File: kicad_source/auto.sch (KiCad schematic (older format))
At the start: 24 parts, among them U14 NE555, U15 74xx175, U16 74xx00, U17 74xx175, U18 74xx32, U3 74xx08

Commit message: added pause mode for automate
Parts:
- U14: symbol IC_logic:NE555 -> SonarExtenderI2C-rescue:NE555-IC_logic
- U15, U17: symbol IC_logic:74xx175 -> SonarExtenderI2C-rescue:74xx175-IC_logic
- U16: symbol IC_logic:74xx00 -> SonarExtenderI2C-rescue:74xx00-IC_logic
- U18: symbol IC_logic:74xx32 -> SonarExtenderI2C-rescue:74xx32-IC_logic
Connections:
- net labels added: AUTOEN, PAUSE
- net labels removed: CNT0, CNT1, CNT2, CNT3
- wire segments 175 -> 170
- no-connect marks 5 -> 11
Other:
- moved on the sheet: C15, C16, C17, C21, R3, R4, U3

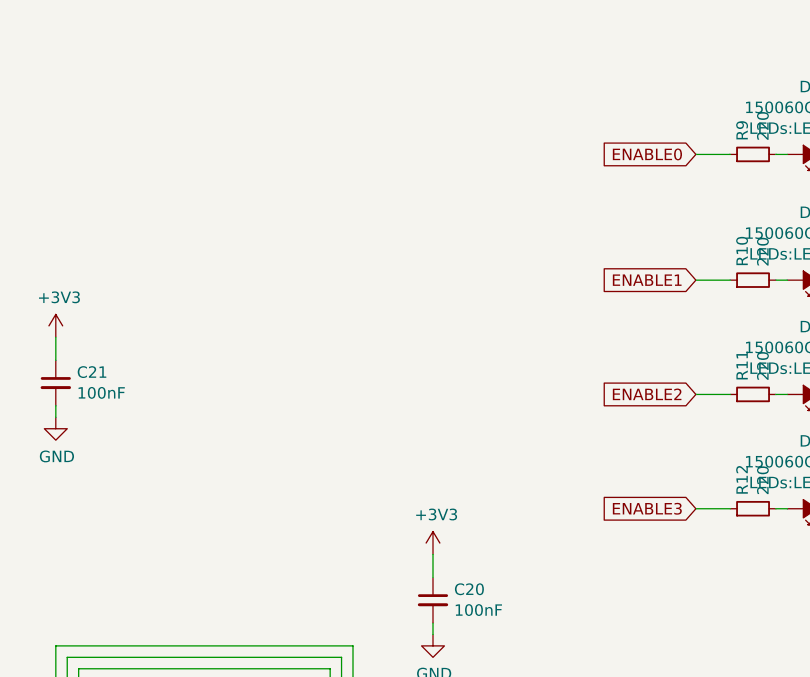
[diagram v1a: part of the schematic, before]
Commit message: added EN LEDS
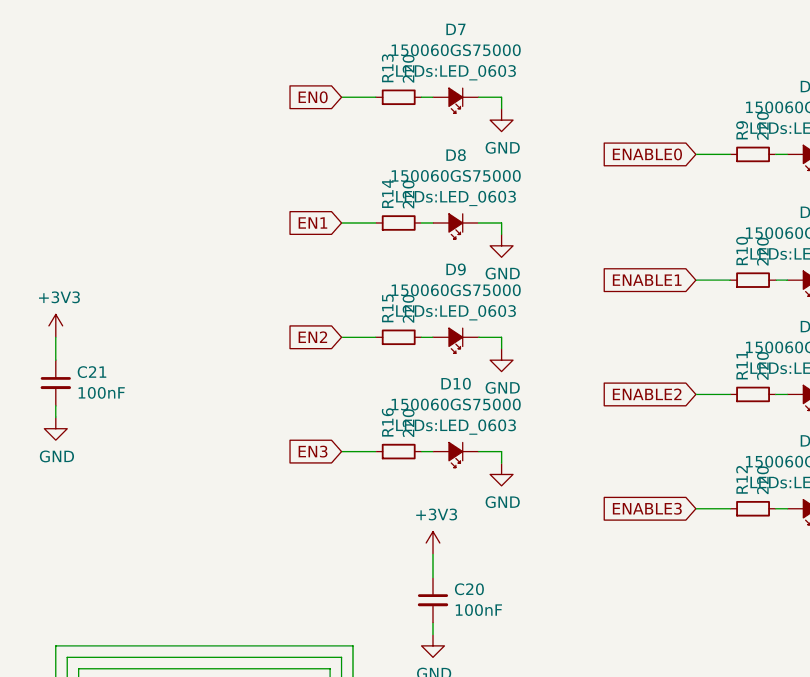
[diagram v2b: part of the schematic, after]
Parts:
- added D10, D7, D8, D9: 150060GS75000, LEDs:LED_0603, symbol devices:Led_Small
- added R13, R14, R15, R16: 220, resistors:R_0603, symbol devices:R_0603
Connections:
- wire segments 170 -> 186
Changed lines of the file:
@@
 NoConn ~ 3550 2500
 NoConn ~ 3550 2300
+$Comp
+L devices:R_0603 R?
+U 1 1 5F04A413
+P 8150 950
+AR Path="/5F04A413" Ref="R?"  Part="1"
+AR Path="/5EDDA6D0/5F04A413" Ref="R13"  Part="1"
+F 0 "R13" H 8209 996 50  0000 L CNN
+F 1 "220" H 8209 905 50  0000 L CNN
+F 2 "resistors:R_0603" H 8150 800 50  0001 C CNN
+F 3 "" H 8150 950 50  0000 C CNN
+	1    8150 950
+	0    -1   -1   0
+$EndComp
+Wire Wire Line
+	8300 950  8250 950
+$Comp
+L power-supply:GND #PWR?
+U 1 1 5F04A41A
+P 8600 1000
+AR Path="/5F04A41A" Ref="#PWR?"  Part="1"
+AR Path="/5EDDA6D0/5F04A41A" Ref="#PWR0132"  Part="1"
+F 0 "#PWR0132" H 8600 750 50  0001 C CNN
+F 1 "GND" H 8605 827 50  0000 C CNN
+F 2 "" H 8600 1000 50  0000 C CNN
+F 3 "" H 8600 1000 50  0000 C CNN
+	1    8600 1000
+	1    0    0    -1
+$EndComp
+Wire Wire Line
+	8600 950  8600 1000
+Wire Wire Line
+	8500 950  8600 950
+$Comp
+L devices:R_0603 R?
+U 1 1 5F04A422
+P 8150 1500
+AR Path="/5F04A422" Ref="R?"  Part="1"
+AR Path="/5EDDA6D0/5F04A422" Ref="R14"  Part="1"
+F 0 "R14" H 8209 1546 50  0000 L CNN
+F 1 "220" H 8209 1455 50  0000 L CNN
+F 2 "resistors:R_0603" H 8150 1350 50  0001 C CNN
+F 3 "" H 8150 1500 50  0000 C CNN
+	1    8150 1500
+	0    -1   -1   0
+$EndComp
+Wire Wire Line
+	8300 1500 8250 1500
+$Comp
+L power-supply:GND #PWR?
+U 1 1 5F04A429
+P 8600 1550
+AR Path="/5F04A429" Ref="#PWR?"  Part="1"
+AR Path="/5EDDA6D0/5F04A429" Ref="#PWR0133"  Part="1"
+F 0 "#PWR0133" H 8600 1300 50  0001 C CNN
+F 1 "GND" H 8605 1377 50  0000 C CNN
+F 2 "" H 8600 1550 50  0000 C CNN
+F 3 "" H 8600 1550 50  0000 C CNN
+	1    8600 1550
+	1    0    0    -1
+$EndComp
+Wire Wire Line
+	8600 1500 8600 1550
+Wire Wire Line
+	8500 1500 8600 1500
+$Comp
+L devices:R_0603 R?
+U 1 1 5F04A431
+P 8150 2000
+AR Path="/5F04A431" Ref="R?"  Part="1"
+AR Path="/5EDDA6D0/5F04A431" Ref="R15"  Part="1"
+F 0 "R15" H 8209 2046 50  0000 L CNN
+F 1 "220" H 8209 1955 50  0000 L CNN
+F 2 "resistors:R_0603" H 8150 1850 50  0001 C CNN
+F 3 "" H 8150 2000 50  0000 C CNN
+	1    8150 2000
+	0    -1   -1   0
+$EndComp
+Wire Wire Line
+	8300 2000 8250 2000
+$Comp
+L power-supply:GND #PWR?
+U 1 1 5F04A438
+P 8600 2050
+AR Path="/5F04A438" Ref="#PWR?"  Part="1"
+AR Path="/5EDDA6D0/5F04A438" Ref="#PWR0134"  Part="1"
+F 0 "#PWR0134" H 8600 1800 50  0001 C CNN
+F 1 "GND" H 8605 1877 50  0000 C CNN
+F 2 "" H 8600 2050 50  0000 C CNN
+F 3 "" H 8600 2050 50  0000 C CNN
+	1    8600 2050
+	1    0    0    -1
+$EndComp
+Wire Wire Line
+	8600 2000 8600 2050
+Wire Wire Line
+	8500 2000 8600 2000
+$Comp
+L devices:R_0603 R?
+U 1 1 5F04A440
+P 8150 2500
+AR Path="/5F04A440" Ref="R?"  Part="1"
+AR Path="/5EDDA6D0/5F04A440" Ref="R16"  Part="1"
+F 0 "R16" H 8209 2546 50  0000 L CNN
+F 1 "220" H 8209 2455 50  0000 L CNN
+F 2 "resistors:R_0603" H 8150 2350 50  0001 C CNN
+F 3 "" H 8150 2500 50  0000 C CNN
+	1    8150 2500
+	0    -1   -1   0
+$EndComp
+$Comp
+L devices:Led_Small D?
+U 1 1 5F04A446
+P 8400 2500
+AR Path="/5F04A446" Ref="D?"  Part="1"
+AR Path="/5EDDA6D0/5F04A446" Ref="D10"  Part="1"
+F 0 "D10" H 8400 2205 50  0000 C CNN
+F 1 "150060GS75000" H 8400 2296 50  0000 C CNN
+F 2 "LEDs:LED_0603" H 8400 2387 50  0000 C CNN
+F 3 "" V 8400 2500 50  0000 C CNN
+	1    8400 2500
+	-1   0    0    1
+$EndComp
+Wire Wire Line
+	8300 2500 8250 2500
+$Comp
+L power-supply:GND #PWR?
+U 1 1 5F04A44D
+P 8600 2550
+AR Path="/5F04A44D" Ref="#PWR?"  Part="1"
+AR Path="/5EDDA6D0/5F04A44D" Ref="#PWR0135"  Part="1"
+F 0 "#PWR0135" H 8600 2300 50  0001 C CNN
+F 1 "GND" H 8605 2377 50  0000 C CNN
+F 2 "" H 8600 2550 50  0000 C CNN
+F 3 "" H 8600 2550 50  0000 C CNN
+	1    8600 2550
+	1    0    0    -1
+$EndComp
+Wire Wire Line
+	8600 2500 8600 2550
+Wire Wire Line
+	8500 2500 8600 2500
+Wire Wire Line
+	8050 2500 7900 2500
+Wire Wire Line
+	8050 2000 7900 2000
+Wire Wire Line
+	8050 1500 7900 1500
+Wire Wire Line
+	8050 950  7900 950
+Text GLabel 7900 950  0    50   Input ~ 0
+EN0
+Text GLabel 7900 1500 0    50   Input ~ 0
+EN1
+Text GLabel 7900 2000 0    50   Input ~ 0
+EN2
+Text GLabel 7900 2500 0    50   Input ~ 0
+EN3
+$Comp
+L devices:Led_Small D?
+U 1 1 5F04A45D
+P 8400 2000
+AR Path="/5F04A45D" Ref="D?"  Part="1"
+AR Path="/5EDDA6D0/5F04A45D" Ref="D9"  Part="1"
+F 0 "D9" H 8400 1705 50  0000 C CNN
+F 1 "150060GS75000" H 8400 1796 50  0000 C CNN
+F 2 "LEDs:LED_0603" H 8400 1887 50  0000 C CNN
+F 3 "" V 8400 2000 50  0000 C CNN
+	1    8400 2000
+	-1   0    0    1
+$EndComp
+$Comp
+L devices:Led_Small D?
+U 1 1 5F04A463
+P 8400 1500
+AR Path="/5F04A463" Ref="D?"  Part="1"
+AR Path="/5EDDA6D0/5F04A463" Ref="D8"  Part="1"
+F 0 "D8" H 8400 1205 50  0000 C CNN
+F 1 "150060GS75000" H 8400 1296 50  0000 C CNN
+F 2 "LEDs:LED_0603" H 8400 1387 50  0000 C CNN
+F 3 "" V 8400 1500 50  0000 C CNN
+	1    8400 1500
+	-1   0    0    1
+$EndComp
+$Comp
+L devices:Led_Small D?
+U 1 1 5F04A469
+P 8400 950
+AR Path="/5F04A469" Ref="D?"  Part="1"
+AR Path="/5EDDA6D0/5F04A469" Ref="D7"  Part="1"
+F 0 "D7" H 8400 655 50  0000 C CNN
+F 1 "150060GS75000" H 8400 746 50  0000 C CNN
+F 2 "LEDs:LED_0603" H 8400 837 50  0000 C CNN
+F 3 "" V 8400 950 50  0000 C CNN
+	1    8400 950
+	-1   0    0    1
+$EndComp
 $EndSCHEMATC

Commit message: updated schematics
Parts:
- removed C18, C19, C20, C21: 100nF, capacitors:C_0603, symbol devices:C_0603
- removed U15, U17: 74xx175, SOIC:SOIC-16_3.9x9.9mm_Pitch1.27mm, symbol SonarExtenderI2C-rescue:74xx175-IC_logic
- removed U16: 74xx00, SOIC:SOIC-14_3.9x8.7mm_Pitch1.27mm, symbol SonarExtenderI2C-rescue:74xx00-IC_logic
- removed U3: 74xx08, SOIC:SOIC-14_3.9x8.7mm_Pitch1.27mm, symbol IC_logic:74xx08
- added C? (x4): 100nF, capacitors:C_0603, symbol devices:C_0603
- added U?: 74xx590-IC_logic, SOIC:SOIC-16_3.9x9.9mm_Pitch1.27mm, symbol SonarExtenderI2C-rescue:74xx590-IC_logic
- added U?: 74xx138-IC_logic, SOIC:SOIC-16_3.9x9.9mm_Pitch1.27mm, symbol SonarExtenderI2C-rescue:74xx138-IC_logic
- added U?: 74xx02, SOIC:SOIC-14_3.9x8.7mm_Pitch1.27mm, symbol IC_logic:74xx02
- added U?: 74xx00, SOIC:SOIC-14_3.9x8.7mm_Pitch1.27mm, symbol IC_logic:74xx00
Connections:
- net labels added: AUTO_INT, AUTO_RESET, CLK_10HZ, RES, ~AUTO_RES, ~E0, ~E1, ~E2, ~E3, ~INT, ~RES
- net labels removed: AUTOEN, CLK_10Hz, E0#, E1#, E2#, E3#, I2C_INT, PAUSE, Q3#
- wire segments 186 -> 171
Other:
- note removed: "COUNTER PRESET"
- note removed: "RING COUNTER"

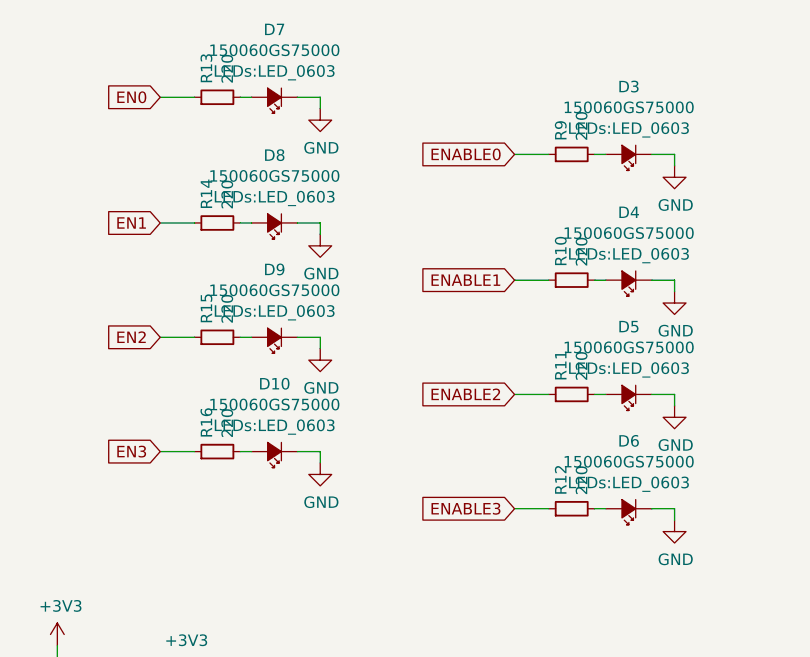
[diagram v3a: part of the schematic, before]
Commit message: solved issues in schematics
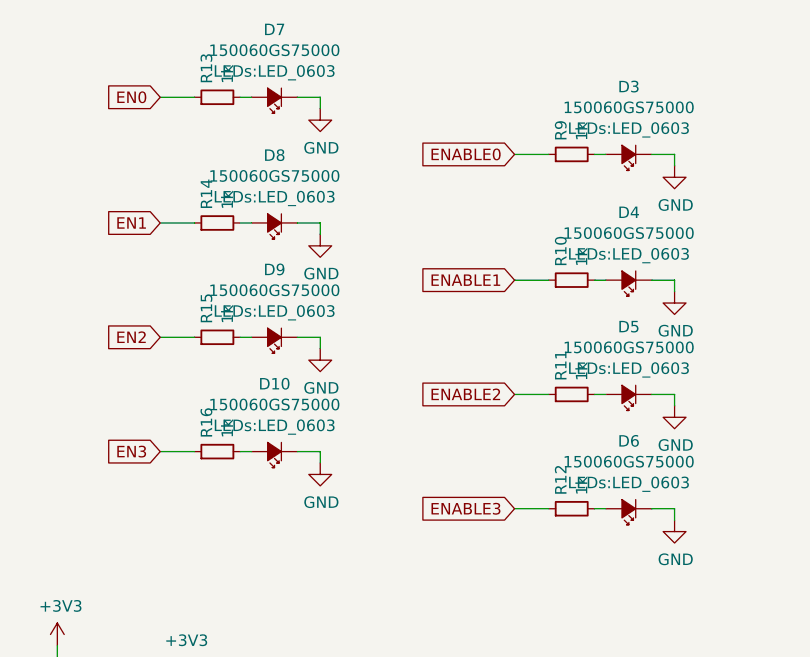
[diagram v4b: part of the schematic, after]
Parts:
- R10, R11, R12, R13, R14, R15, R16, R9: value 220 -> 1k
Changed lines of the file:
@@
 AR Path="/5EDDA6D0/5EF55645" Ref="R9"  Part="1"
 F 0 "R9" H 9759 1246 50  0000 L CNN
-F 1 "220" H 9759 1155 50  0000 L CNN
+F 1 "1k" H 9759 1155 50  0000 L CNN
 F 2 "resistors:R_0603" H 9700 1050 50  0001 C CNN
 F 3 "" H 9700 1200 50  0000 C CNN
@@
 AR Path="/5EDDA6D0/5EF6B354" Ref="R10"  Part="1"
 F 0 "R10" H 9759 1796 50  0000 L CNN
-F 1 "220" H 9759 1705 50  0000 L CNN
+F 1 "1k" H 9759 1705 50  0000 L CNN
 F 2 "resistors:R_0603" H 9700 1600 50  0001 C CNN
 F 3 "" H 9700 1750 50  0000 C CNN
@@
 AR Path="/5EDDA6D0/5EF72572" Ref="R11"  Part="1"
 F 0 "R11" H 9759 2296 50  0000 L CNN
-F 1 "220" H 9759 2205 50  0000 L CNN
+F 1 "1k" H 9759 2205 50  0000 L CNN
 F 2 "resistors:R_0603" H 9700 2100 50  0001 C CNN
 F 3 "" H 9700 2250 50  0000 C CNN
@@
 AR Path="/5EDDA6D0/5EF795B4" Ref="R12"  Part="1"
 F 0 "R12" H 9759 2796 50  0000 L CNN
-F 1 "220" H 9759 2705 50  0000 L CNN
+F 1 "1k" H 9759 2705 50  0000 L CNN
 F 2 "resistors:R_0603" H 9700 2600 50  0001 C CNN
 F 3 "" H 9700 2750 50  0000 C CNN
@@
 AR Path="/5EDDA6D0/5F04A413" Ref="R13"  Part="1"
 F 0 "R13" H 8209 996 50  0000 L CNN
-F 1 "220" H 8209 905 50  0000 L CNN
+F 1 "1k" H 8209 905 50  0000 L CNN
 F 2 "resistors:R_0603" H 8150 800 50  0001 C CNN
 F 3 "" H 8150 950 50  0000 C CNN
@@
 AR Path="/5EDDA6D0/5F04A422" Ref="R14"  Part="1"
 F 0 "R14" H 8209 1546 50  0000 L CNN
-F 1 "220" H 8209 1455 50  0000 L CNN
+F 1 "1k" H 8209 1455 50  0000 L CNN
 F 2 "resistors:R_0603" H 8150 1350 50  0001 C CNN
 F 3 "" H 8150 1500 50  0000 C CNN
@@
 AR Path="/5EDDA6D0/5F04A431" Ref="R15"  Part="1"
 F 0 "R15" H 8209 2046 50  0000 L CNN
-F 1 "220" H 8209 1955 50  0000 L CNN
+F 1 "1k" H 8209 1955 50  0000 L CNN
 F 2 "resistors:R_0603" H 8150 1850 50  0001 C CNN
 F 3 "" H 8150 2000 50  0000 C CNN
@@
 AR Path="/5EDDA6D0/5F04A440" Ref="R16"  Part="1"
 F 0 "R16" H 8209 2546 50  0000 L CNN
-F 1 "220" H 8209 2455 50  0000 L CNN
+F 1 "1k" H 8209 2455 50  0000 L CNN
 F 2 "resistors:R_0603" H 8150 2350 50  0001 C CNN
 F 3 "" H 8150 2500 50  0000 C CNN
